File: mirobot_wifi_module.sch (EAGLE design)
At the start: 4 parts

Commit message: Version 1.4 of the mian PCB and 1.1 of the WiFi PCB
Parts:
- JP1: device pinhead:PINHD-1X4/90 -> Child-Friendly-Parts:PINHD-2X3
- R1, R2: device rcl:R-EU_0204/5 -> Child-Friendly-Parts:R-EU_0204/5
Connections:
- new net N$6: JP1.5, U$1.NREADY
- new net N$7: JP1.6, U$1.EXT_RESET
- net N$2: now also JP1.2; no longer JP1.4
- net N$3: now also JP1.4; no longer JP1.3
- net N$5: now also JP1.3; no longer JP1.2
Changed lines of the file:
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@@
 <parts>
 <part name="U$1" library="usr_wifi" deviceset="USR_WIFI" device=""/>
-<part name="JP1" library="pinhead" deviceset="PINHD-1X4" device="/90"/>
-<part name="R1" library="rcl" deviceset="R-EU_" device="0204/5" value="50K"/>
-<part name="R2" library="rcl" deviceset="R-EU_" device="0204/5" value="100K"/>
+<part name="R1" library="Child-Friendly-Parts" deviceset="R-EU_" device="0204/5" value="50K"/>
+<part name="R2" library="Child-Friendly-Parts" deviceset="R-EU_" device="0204/5" value="100K"/>
+<part name="JP1" library="Child-Friendly-Parts" deviceset="PINHD-2X3" device=""/>
 </parts>
 <sheets>
@@
 <instances>
 <instance part="U$1" gate="G$1" x="60.96" y="43.18"/>
-<instance part="JP1" gate="A" x="71.12" y="-7.62" rot="R270"/>
 <instance part="R1" gate="G$1" x="114.3" y="55.88"/>
 <instance part="R2" gate="G$1" x="30.48" y="53.34"/>
+<instance part="JP1" gate="A" x="73.66" y="-10.16"/>
 </instances>
 <busses>
@@
 <pinref part="U$1" gate="G$1" pin="GND"/>
 <wire x1="45.72" y1="66.04" x2="20.32" y2="66.04" width="0.1524" layer="91"/>
-<wire x1="20.32" y1="66.04" x2="20.32" y2="2.54" width="0.1524" layer="91"/>
-<wire x1="76.2" y1="2.54" x2="20.32" y2="2.54" width="0.1524" layer="91"/>
+<wire x1="20.32" y1="66.04" x2="20.32" y2="-7.62" width="0.1524" layer="91"/>
+<wire x1="71.12" y1="-7.62" x2="20.32" y2="-7.62" width="0.1524" layer="91"/>
 <pinref part="JP1" gate="A" pin="1"/>
-<wire x1="76.2" y1="2.54" x2="76.2" y2="-5.08" width="0.1524" layer="91"/>
 </segment>
 </net>
@@
 <pinref part="U$1" gate="G$1" pin="DVDD"/>
 <wire x1="22.86" y1="48.26" x2="45.72" y2="48.26" width="0.1524" layer="91"/>
-<wire x1="22.86" y1="0" x2="68.58" y2="0" width="0.1524" layer="91"/>
-<pinref part="JP1" gate="A" pin="4"/>
-<wire x1="68.58" y1="0" x2="68.58" y2="-5.08" width="0.1524" layer="91"/>
 <pinref part="R2" gate="G$1" pin="1"/>
 <wire x1="25.4" y1="53.34" x2="22.86" y2="53.34" width="0.1524" layer="91"/>
@@
 <pinref part="R1" gate="G$1" pin="2"/>
 <wire x1="119.38" y1="55.88" x2="119.38" y2="0" width="0.1524" layer="91"/>
-<wire x1="68.58" y1="0" x2="119.38" y2="0" width="0.1524" layer="91"/>
-<junction x="68.58" y="0"/>
+<wire x1="22.86" y1="0" x2="86.36" y2="0" width="0.1524" layer="91"/>
+<pinref part="JP1" gate="A" pin="2"/>
+<wire x1="86.36" y1="0" x2="119.38" y2="0" width="0.1524" layer="91"/>
+<wire x1="78.74" y1="-7.62" x2="86.36" y2="-7.62" width="0.1524" layer="91"/>
+<wire x1="86.36" y1="-7.62" x2="86.36" y2="0" width="0.1524" layer="91"/>
+<junction x="86.36" y="0"/>
 </segment>
 </net>
@@
 <pinref part="U$1" gate="G$1" pin="UART0_RX"/>
 <wire x1="99.06" y1="45.72" x2="114.3" y2="45.72" width="0.1524" layer="91"/>
-<wire x1="114.3" y1="45.72" x2="114.3" y2="7.62" width="0.1524" layer="91"/>
-<wire x1="71.12" y1="7.62" x2="114.3" y2="7.62" width="0.1524" layer="91"/>
-<pinref part="JP1" gate="A" pin="3"/>
-<wire x1="71.12" y1="7.62" x2="71.12" y2="-5.08" width="0.1524" layer="91"/>
+<wire x1="114.3" y1="45.72" x2="114.3" y2="-10.16" width="0.1524" layer="91"/>
+<wire x1="78.74" y1="-10.16" x2="114.3" y2="-10.16" width="0.1524" layer="91"/>
+<pinref part="JP1" gate="A" pin="4"/>
 </segment>
 </net>
 <net name="N$5" class="0">
 <segment>
-<wire x1="73.66" y1="5.08" x2="111.76" y2="5.08" width="0.1524" layer="91"/>
+<wire x1="60.96" y1="5.08" x2="111.76" y2="5.08" width="0.1524" layer="91"/>
 <wire x1="111.76" y1="5.08" x2="111.76" y2="40.64" width="0.1524" layer="91"/>
 <pinref part="U$1" gate="G$1" pin="UART0_TX"/>
 <wire x1="111.76" y1="40.64" x2="99.06" y2="40.64" width="0.1524" layer="91"/>
-<pinref part="JP1" gate="A" pin="2"/>
-<wire x1="73.66" y1="5.08" x2="73.66" y2="-5.08" width="0.1524" layer="91"/>
+<wire x1="60.96" y1="5.08" x2="60.96" y2="-10.16" width="0.1524" layer="91"/>
+<pinref part="JP1" gate="A" pin="3"/>
+<wire x1="60.96" y1="-10.16" x2="71.12" y2="-10.16" width="0.1524" layer="91"/>
 </segment>
 </net>
@@
 </segment>
 </net>
+<net name="N$6" class="0">
+<segment>
+<pinref part="U$1" gate="G$1" pin="NREADY"/>
+<wire x1="99.06" y1="53.34" x2="109.22" y2="53.34" width="0.1524" layer="91"/>
+<wire x1="109.22" y1="53.34" x2="109.22" y2="2.54" width="0.1524" layer="91"/>
+<wire x1="109.22" y1="2.54" x2="58.42" y2="2.54" width="0.1524" layer="91"/>
+<wire x1="58.42" y1="2.54" x2="58.42" y2="-12.7" width="0.1524" layer="91"/>
+<pinref part="JP1" gate="A" pin="5"/>
+<wire x1="58.42" y1="-12.7" x2="71.12" y2="-12.7" width="0.1524" layer="91"/>
+</segment>
+</net>
+<net name="N$7" class="0">
+<segment>
+<pinref part="U$1" gate="G$1" pin="EXT_RESET"/>
+<wire x1="99.06" y1="60.96" x2="121.92" y2="60.96" width="0.1524" layer="91"/>
+<wire x1="121.92" y1="60.96" x2="121.92" y2="-12.7" width="0.1524" layer="91"/>
+<wire x1="121.92" y1="-12.7" x2="78.74" y2="-12.7" width="0.1524" layer="91"/>
+<pinref part="JP1" gate="A" pin="6"/>
+</segment>
+</net>

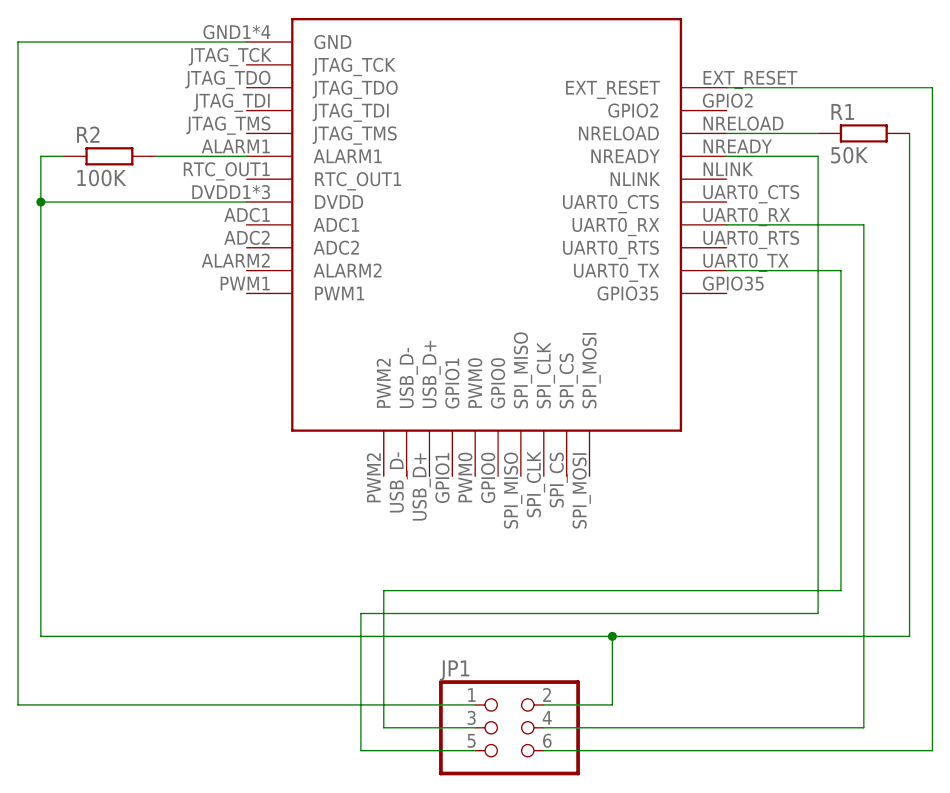
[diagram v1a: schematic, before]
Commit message: Fix crossed RX and TX lines on the WiFi module
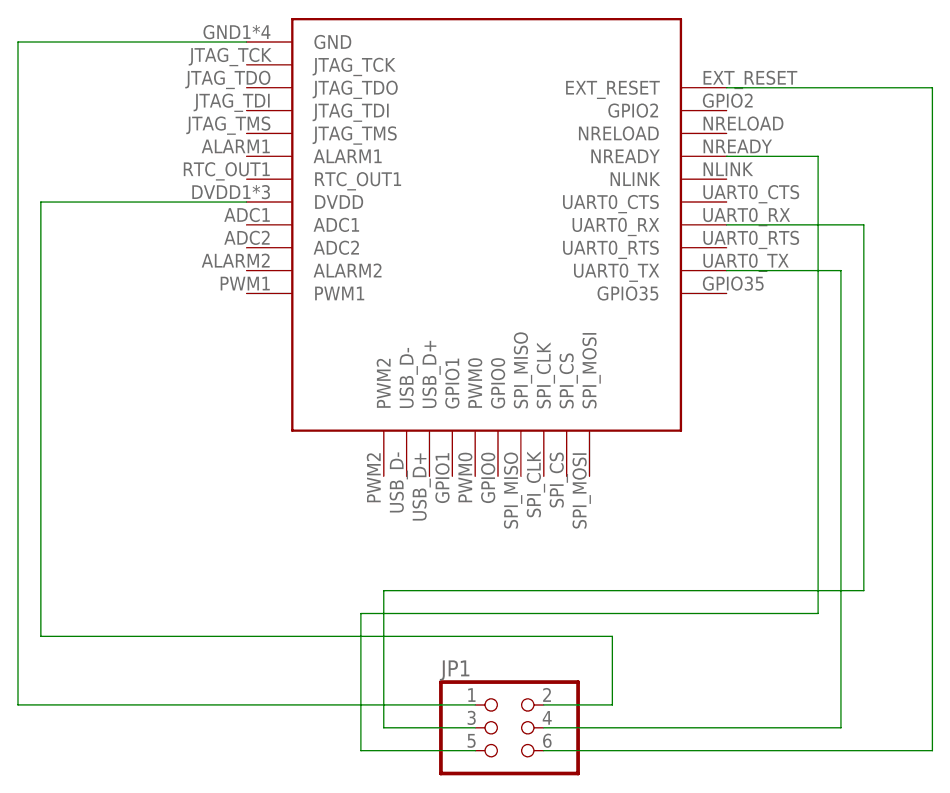
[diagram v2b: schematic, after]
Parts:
- removed R1: 50K, Child-Friendly-Parts:R-EU_0204/5
- removed R2: 100K, Child-Friendly-Parts:R-EU_0204/5
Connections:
- removed net N$1: R2.2, U$1.ALARM1
- removed net N$4: R1.1, U$1.NRELOAD
- net N$2: no longer R1.2, R2.1
- net N$3: now also JP1.3; no longer JP1.4
- net N$5: now also JP1.4; no longer JP1.3
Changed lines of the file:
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@@
 <parts>
 <part name="U$1" library="usr_wifi" deviceset="USR_WIFI" device=""/>
-<part name="R1" library="Child-Friendly-Parts" deviceset="R-EU_" device="0204/5" value="50K"/>
-<part name="R2" library="Child-Friendly-Parts" deviceset="R-EU_" device="0204/5" value="100K"/>
 <part name="JP1" library="Child-Friendly-Parts" deviceset="PINHD-2X3" device=""/>
 </parts>
@@
 <instances>
 <instance part="U$1" gate="G$1" x="60.96" y="43.18"/>
-<instance part="R1" gate="G$1" x="114.3" y="55.88"/>
-<instance part="R2" gate="G$1" x="30.48" y="53.34"/>
 <instance part="JP1" gate="A" x="73.66" y="-10.16"/>
 </instances>
@@
 <pinref part="U$1" gate="G$1" pin="DVDD"/>
 <wire x1="22.86" y1="48.26" x2="45.72" y2="48.26" width="0.1524" layer="91"/>
-<pinref part="R2" gate="G$1" pin="1"/>
-<wire x1="25.4" y1="53.34" x2="22.86" y2="53.34" width="0.1524" layer="91"/>
-<wire x1="22.86" y1="53.34" x2="22.86" y2="48.26" width="0.1524" layer="91"/>
-<junction x="22.86" y="48.26"/>
-<pinref part="R1" gate="G$1" pin="2"/>
-<wire x1="119.38" y1="55.88" x2="119.38" y2="0" width="0.1524" layer="91"/>
 <wire x1="22.86" y1="0" x2="86.36" y2="0" width="0.1524" layer="91"/>
 <pinref part="JP1" gate="A" pin="2"/>
-<wire x1="86.36" y1="0" x2="119.38" y2="0" width="0.1524" layer="91"/>
 <wire x1="78.74" y1="-7.62" x2="86.36" y2="-7.62" width="0.1524" layer="91"/>
 <wire x1="86.36" y1="-7.62" x2="86.36" y2="0" width="0.1524" layer="91"/>
-<junction x="86.36" y="0"/>
 </segment>
 </net>
@@
 <pinref part="U$1" gate="G$1" pin="UART0_RX"/>
 <wire x1="99.06" y1="45.72" x2="114.3" y2="45.72" width="0.1524" layer="91"/>
-<wire x1="114.3" y1="45.72" x2="114.3" y2="-10.16" width="0.1524" layer="91"/>
-<wire x1="78.74" y1="-10.16" x2="114.3" y2="-10.16" width="0.1524" layer="91"/>
-<pinref part="JP1" gate="A" pin="4"/>
-</segment>
-</net>
-<net name="N$5" class="0">
-<segment>
-<wire x1="60.96" y1="5.08" x2="111.76" y2="5.08" width="0.1524" layer="91"/>
-<wire x1="111.76" y1="5.08" x2="111.76" y2="40.64" width="0.1524" layer="91"/>
-<pinref part="U$1" gate="G$1" pin="UART0_TX"/>
-<wire x1="111.76" y1="40.64" x2="99.06" y2="40.64" width="0.1524" layer="91"/>
+<wire x1="114.3" y1="45.72" x2="114.3" y2="5.08" width="0.1524" layer="91"/>
+<wire x1="114.3" y1="5.08" x2="60.96" y2="5.08" width="0.1524" layer="91"/>
 <wire x1="60.96" y1="5.08" x2="60.96" y2="-10.16" width="0.1524" layer="91"/>
 <pinref part="JP1" gate="A" pin="3"/>
@@
 </segment>
 </net>
-<net name="N$1" class="0">
+<net name="N$5" class="0">
 <segment>
-<pinref part="U$1" gate="G$1" pin="ALARM1"/>
-<pinref part="R2" gate="G$1" pin="2"/>
-<wire x1="45.72" y1="53.34" x2="35.56" y2="53.34" width="0.1524" layer="91"/>
+<wire x1="111.76" y1="-10.16" x2="111.76" y2="40.64" width="0.1524" layer="91"/>
+<pinref part="U$1" gate="G$1" pin="UART0_TX"/>
+<wire x1="111.76" y1="40.64" x2="99.06" y2="40.64" width="0.1524" layer="91"/>
+<pinref part="JP1" gate="A" pin="4"/>
+<wire x1="78.74" y1="-10.16" x2="111.76" y2="-10.16" width="0.1524" layer="91"/>
 </segment>
 </net>
-<net name="N$4" class="0">
-<segment>
-<pinref part="U$1" gate="G$1" pin="NRELOAD"/>
-<pinref part="R1" gate="G$1" pin="1"/>
-<wire x1="99.06" y1="55.88" x2="109.22" y2="55.88" width="0.1524" layer="91"/>
-</segment>
-</net>
